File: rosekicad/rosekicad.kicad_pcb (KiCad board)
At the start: 4 copper layers, 190.5 x 165.1 mm, 78 parts, among them J1 Solenoid, J10 Solenoid, J11 Solenoid, J12 Solenoid, J13 UV Lights, J14 LED Lights, J15 DMX Cable, J16 Barrel_Jack_MountingPin, J2 Solenoid, J3 Solenoid, J4 Solenoid, J5 Solenoid, J6 Solenoid, J7 Solenoid, J8 Solenoid, J9 Solenoid, Q1 2N2222, Q10 2N2222, Q11 2N2222, Q12 2N2222, Q13 2N2222, Q14 2N2222, Q15 2N2222, Q2 2N2222, Q3 2N2222, Q4 2N2222, Q5 2N2222, Q6 2N2222, Q7 2N2222, Q8 2N2222, Q9 2N2222, U1 MAX485E

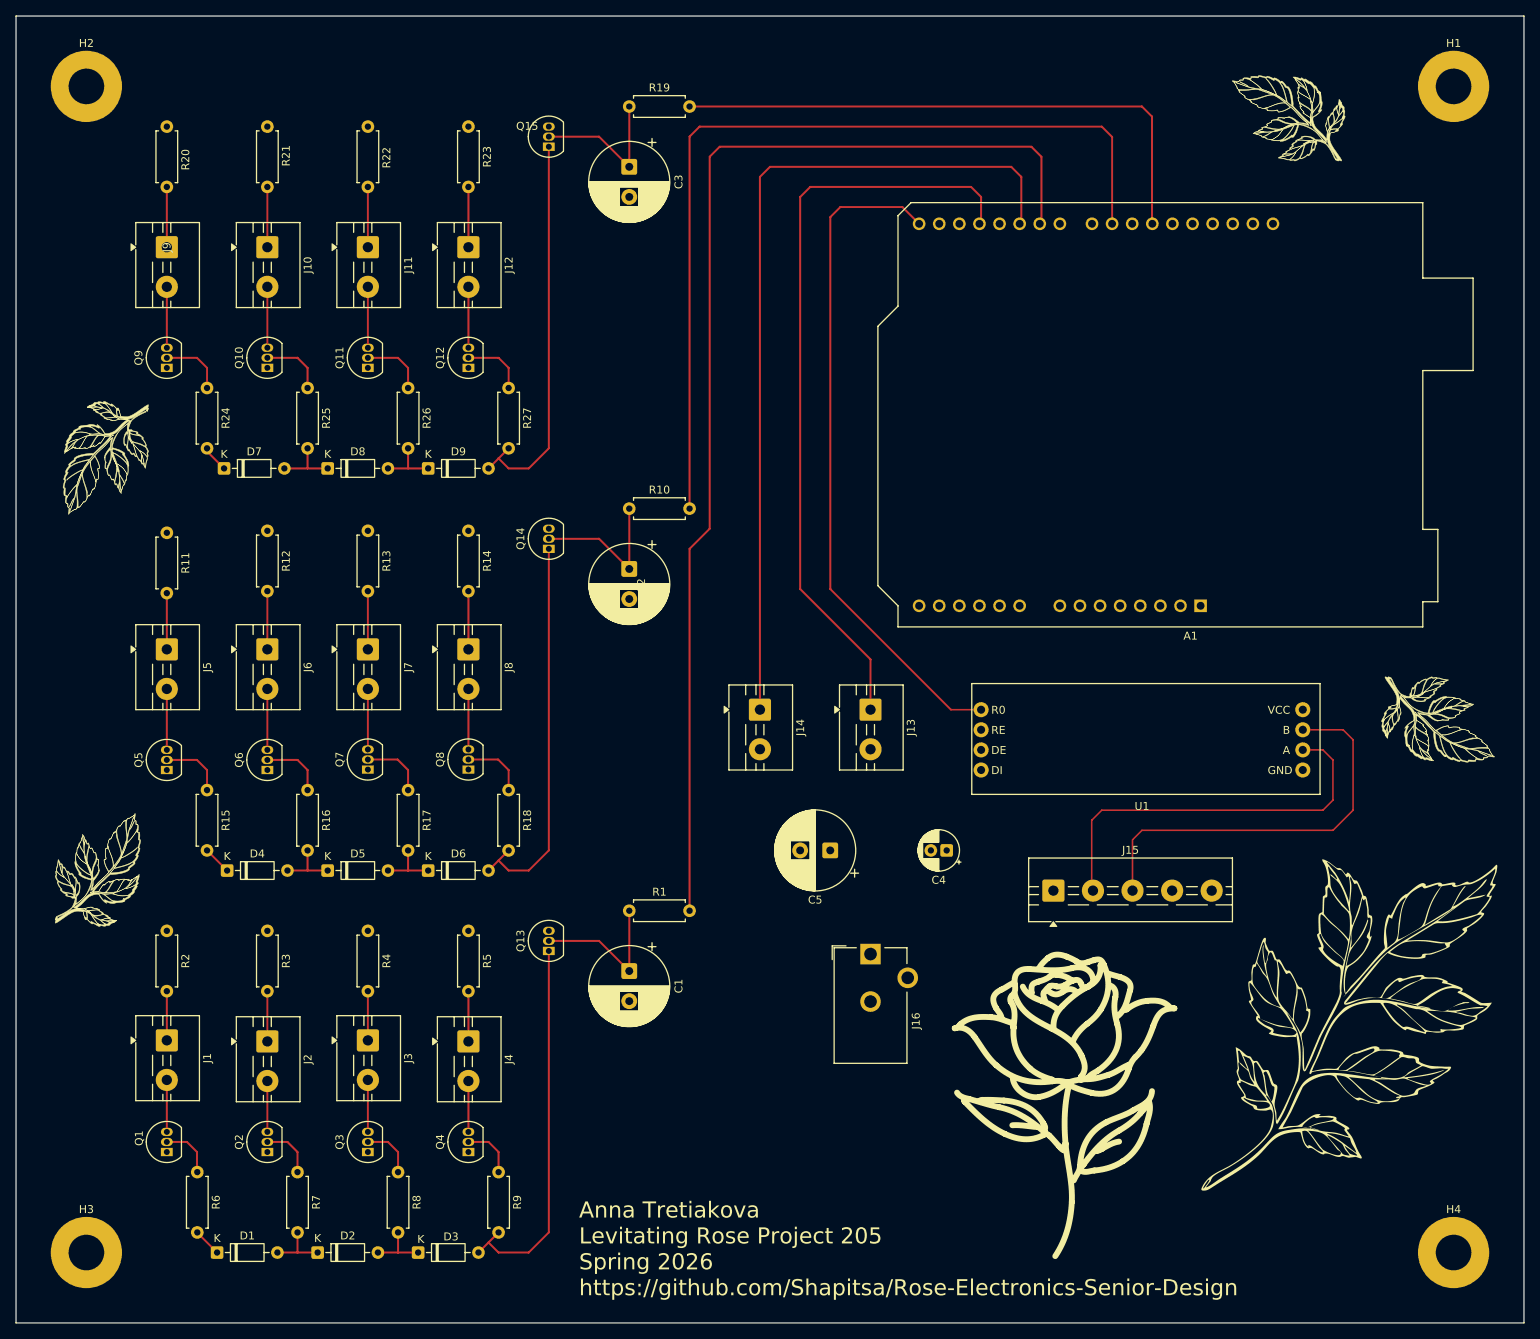
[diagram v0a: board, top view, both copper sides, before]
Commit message: mosfets added
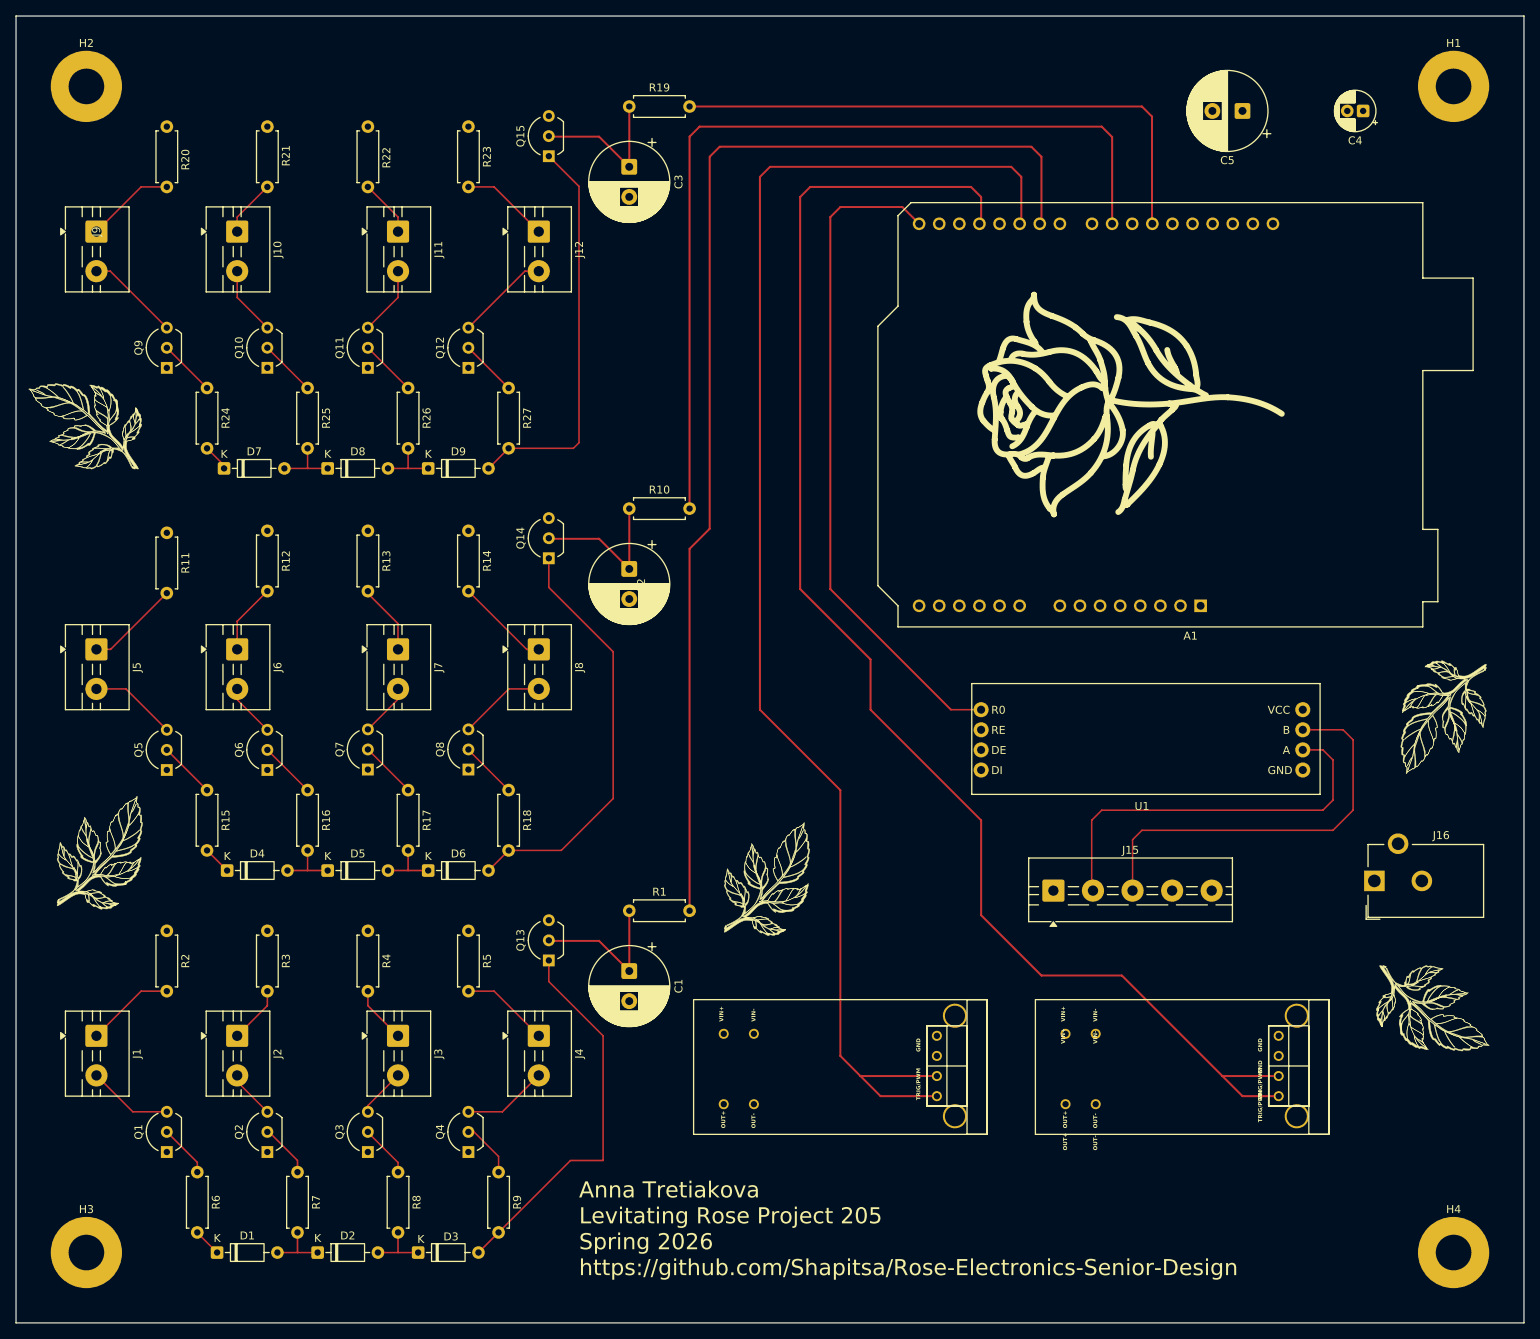
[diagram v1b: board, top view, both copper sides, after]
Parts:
- J13, J14: footprint TerminalBlock:TerminalBlock_MaiXu_MX126-5.0-02P_1x02_P5.00mm -> rosekicad:MOSFET Switch Driver Module
- Q1, Q10, Q11, Q12, Q13, Q14, Q15, Q2, Q3, Q4, Q5, Q6, Q7, Q8, Q9: footprint Package_TO_SOT_THT:TO-92_Inline -> Package_TO_SOT_THT:TO-92_Inline_Wide
- moved C4 107.2 mm to (241.3, 63.5)
- moved C5 107.0 mm to (226.1, 63.5)
- moved J14 73.9 mm to (218.4, 190.2), turned to 90 degrees
- moved J16 64.3 mm to (242.7, 160.8), turned to 90 degrees
- moved J13 51.3 mm to (175.3, 190.2), turned to 90 degrees
- moved J9 9.11 mm to (81.3, 78.7)
- moved J12 9.11 mm to (137.2, 78.7)
- moved J4 8.92 mm to (137.2, 180.3)
- moved J1 8.91 mm to (81.3, 180.3)
- moved J5 8.89 mm to (81.3, 131.5)
- moved J8 8.89 mm to (137.2, 131.5)
- moved J10 4.29 mm to (99.1, 78.7)
- moved J11 4.29 mm to (119.4, 78.7)
- moved J2 3.88 mm to (99.1, 180.3)
- moved J3 3.85 mm to (119.4, 180.3)
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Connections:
- J13 pad 1: Net-(A1-D3) -> unconnected-(J13-OUT+-Pad1)
- J13 pad 2: GND -> unconnected-(J13-OUT--Pad2)
- J14 pad 1: Net-(A1-D5) -> unconnected-(J14-OUT+-Pad1)
- J14 pad 2: GND -> unconnected-(J14-OUT--Pad2)
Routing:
- net Net-(A1-D3): track 95.8 -> 181.8 mm
- net Net-(A1-D5): track 107.4 -> 179.3 mm
- net Net-(J1-Pin_1): track 6.22 -> 11.2 mm
- net Net-(J4-Pin_1): track 6.35 -> 11.2 mm
- net Net-(J5-Pin_1): track 7.10 -> 11.8 mm
- net Net-(J8-Pin_1): track 7.35 -> 11.9 mm
- net Net-(J4-Pin_2): track 6.43 -> 10.8 mm
- net Net-(J1-Pin_2): track 6.56 -> 10.8 mm
- net Net-(J9-Pin_2): track 7.70 -> 11.8 mm
- net Net-(J12-Pin_2): track 7.70 -> 11.8 mm
- net Net-(D6-A): track 49.6 -> 53.2 mm
- net Net-(J9-Pin_1): track 7.62 -> 11.2 mm
- net Net-(J12-Pin_1): track 7.62 -> 11.2 mm
- net Net-(J8-Pin_2): track 7.65 -> 11.0 mm
- net Net-(J5-Pin_2): track 7.70 -> 11.0 mm
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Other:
- board text added: "GND"
- board text added: "OUT+"
- board text added: "OUT-"
- board text added: "TRIG/PWM"
- board text added: "VIN+"
- board text added: "VIN-"

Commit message: final
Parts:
- removed J13: UV Lights, rosekicad:MOSFET Switch Driver Module
- removed J14: LED Lights, rosekicad:MOSFET Switch Driver Module
- added U2: MOSFET_module, rosekicad:MOSFET Switch Driver Module, F.Cu at (219.5, 190.2)
- added U3: MOSFET_module, rosekicad:MOSFET Switch Driver Module, F.Cu at (175.8, 190.2)
- moved J15 56.4 mm to (250.7, 190.8), turned to 90 degrees
- moved J16 3.99 mm to (243.9, 157.0)
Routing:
- net Net-(J15-Pin_2): track 49.9 -> 53.3 mm
- net Net-(A1-D3): track 181.8 -> 183.8 mm
- net Net-(J15-Pin_3): track 51.6 -> 51.1 mm
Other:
- board text removed: "GND"
- board text removed: "OUT+"
- board text removed: "OUT-"
- board text removed: "TRIG/PWM"
- board text removed: "VIN+"
- board text removed: "VIN-"

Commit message: final
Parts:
- R11, R12, R13, R14, R2, R20, R21, R22, R23, R3, R4, R5: footprint Resistor_THT:R_Axial_DIN0207_L6.3mm_D2.5mm_P7.62mm_Horizontal -> Resistor_THT:R_Axial_DIN0414_L11.9mm_D4.5mm_P15.24mm_Horizontal
- moved R5 8.61 mm to (120.1, 164.3), turned to -35 degrees
- moved R23 8.07 mm to (124.6, 58.3), turned to -60 degrees
- moved R4 8.02 mm to (108.0, 164.6), turned to -35 degrees
- moved R22 7.71 mm to (112.8, 58.3), turned to -60 degrees
- moved R20 7.54 mm to (92.5, 58.3), turned to -120 degrees
- moved R21 7.32 mm to (104.3, 58.3), turned to -120 degrees
- moved R13 7.30 mm to (108.7, 114.0), turned to -45 degrees
- moved R14 6.99 mm to (121.8, 113.9), turned to -45 degrees
- moved R2 5.00 mm to (89.2, 162.2), turned to -135 degrees
- moved R12 4.77 mm to (98.8, 114.0), turned to -135 degrees
- moved R11 4.64 mm to (87.0, 113.4), turned to -135 degrees
- moved R3 3.11 mm to (100.6, 165.0), turned to -135 degrees
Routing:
- net Net-(J6-Pin_1): track 8.93 -> 16.1 mm
- net Net-(J2-Pin_1): track 7.22 -> 11.2 mm
- net Net-(J1-Pin_1): track 11.2 -> 8.59 mm
- net Net-(J9-Pin_1): track 11.2 -> 8.72 mm
- net Net-(J7-Pin_1): track 8.93 -> 6.74 mm
- net Net-(J4-Pin_1): track 11.2 -> 9.20 mm
- net Net-(J12-Pin_1): track 11.2 -> 9.30 mm
- net Net-(J8-Pin_1): track 11.9 -> 10.3 mm
- net Net-(J10-Pin_1): track 7.22 -> 8.25 mm
- net Net-(J5-Pin_1): track 11.8 -> 11.2 mm
